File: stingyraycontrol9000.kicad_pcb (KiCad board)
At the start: 2 copper layers, 22.1 x 86.4 mm, 15 parts, among them J1 Screw_Terminal_01x04, J2 Screw_Terminal_01x04, J3 Screw_Terminal_01x02, J4 Conn_01x04, U1 ws2801, U2 LDD-L, U3 LDD-H

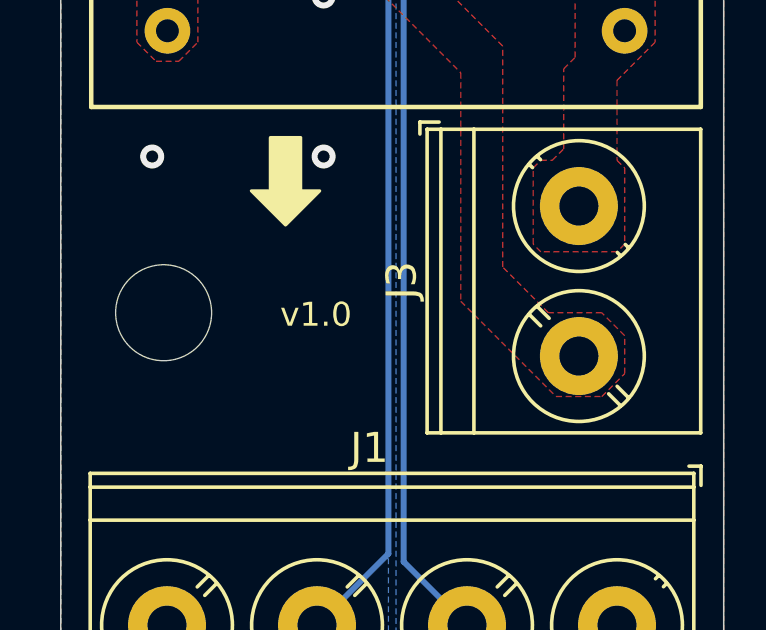
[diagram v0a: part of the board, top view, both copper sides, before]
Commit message: connect WS2801 polarity pin to ground and bump version to 1.1
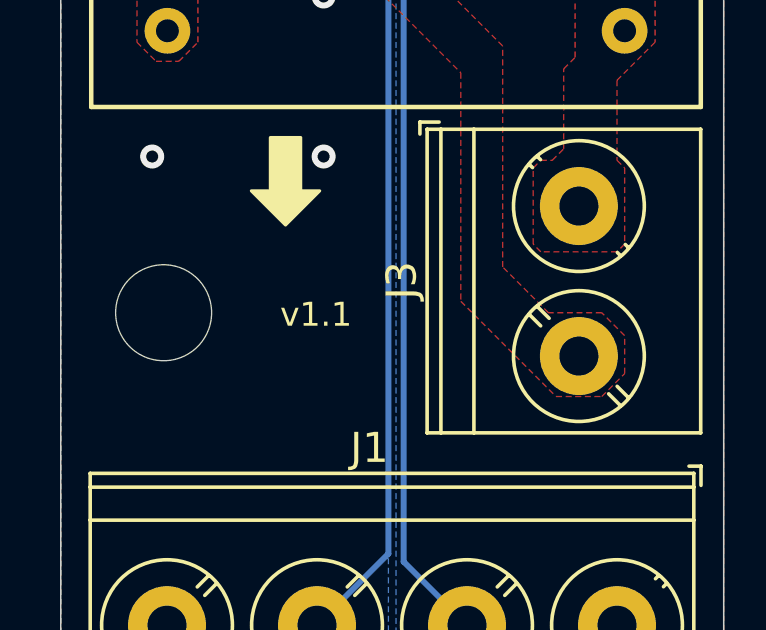
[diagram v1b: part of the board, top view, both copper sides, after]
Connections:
- U1 pad 3: (no net) -> GND
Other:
- board text added: "v1.1"
- board text removed: "v1.0"
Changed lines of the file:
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@@
     (pad 2 smd rect (at -2.7 -2.54) (size 1.5 0.6) (layers F.Cu F.Paste F.Mask)
       (net 2 /SDI))
-    (pad 3 smd rect (at -2.7 -1.27) (size 1.5 0.6) (layers F.Cu F.Paste F.Mask))
+    (pad 3 smd rect (at -2.7 -1.27) (size 1.5 0.6) (layers F.Cu F.Paste F.Mask)
+      (net 3 GND))
     (pad 4 smd rect (at -2.7 0) (size 1.5 0.6) (layers F.Cu F.Paste F.Mask)
       (net 3 GND))
@@
     )
   )
-  (gr_text v1.0 (at 135.001 135.9535) (layer F.SilkS)
+  (gr_text v1.1 (at 135.001 135.9535) (layer F.SilkS)
     (effects (font (size 0.8 0.8) (thickness 0.15)))
   )
@@
   (segment (start 135.048 86.995) (end 135.048 87.075) (width 0.2) (layer B.Cu) (net 1))
   (segment (start 135.255 86.788) (end 135.048 86.995) (width 0.2) (layer B.Cu) (net 1))
-  (segment (start 135.255 70.311) (end 135.255 86.788) (width 0.2) (layer B.Cu) (net 1))
-  (segment (start 135.048 70.104) (end 135.255 70.311) (width 0.2) (layer B.Cu) (net 1))
+  (segment (start 135.255 70.311) (end 135.255 86.788) (width 0.2) (layer B.Cu) (net 1) (status 10))
+  (segment (start 135.048 70.104) (end 135.255 70.311) (width 0.2) (layer B.Cu) (net 1) (status 30))
   (via (at 135.001 88.392) (size 0.6) (drill 0.3) (layers F.Cu B.Cu) (net 2))
   (segment (start 135.001 88.392) (end 133.698 88.392) (width 0.2) (layer F.Cu) (net 2) (status 20))
   (segment (start 135.655011 74.496989) (end 138.748001 71.403999) (width 0.2) (layer B.Cu) (net 2))
   (segment (start 135.001 88.392) (end 135.655011 87.737989) (width 0.2) (layer B.Cu) (net 2))
-  (segment (start 138.748001 71.403999) (end 140.048 70.104) (width 0.2) (layer B.Cu) (net 2))
+  (segment (start 138.748001 71.403999) (end 140.048 70.104) (width 0.2) (layer B.Cu) (net 2) (status 20))
   (segment (start 135.655011 87.737989) (end 135.655011 74.496989) (width 0.2) (layer B.Cu) (net 2))
   (via (at 135.255 125.349) (size 0.8) (drill 0.4) (layers F.Cu B.Cu) (net 3))
@@
   (segment (start 139.098 92.202) (end 142.748 92.202) (width 0.2) (layer F.Cu) (net 6) (status 10))
   (segment (start 147.447 90.297) (end 147.447 101.473) (width 0.2) (layer F.Cu) (net 6))
-  (segment (start 146.049999 102.870001) (end 145.288 103.632) (width 0.2) (layer F.Cu) (net 6))
+  (segment (start 146.049999 102.870001) (end 145.288 103.632) (width 0.2) (layer F.Cu) (net 6) (status 20))
   (segment (start 147.447 101.473) (end 146.049999 102.870001) (width 0.2) (layer F.Cu) (net 6))
-  (segment (start 146.05 88.9) (end 147.447 90.297) (width 0.2) (layer F.Cu) (net 6))
-  (segment (start 143.764 105.156) (end 145.288 103.632) (width 0.2) (layer F.Cu) (net 6))
+  (segment (start 146.05 88.9) (end 147.447 90.297) (width 0.2) (layer F.Cu) (net 6) (status 10))
+  (segment (start 143.764 105.156) (end 145.288 103.632) (width 0.2) (layer F.Cu) (net 6) (status 20))
   (segment (start 139.446 105.156) (end 143.764 105.156) (width 0.2) (layer F.Cu) (net 6))
   (segment (start 137.8966 103.6066) (end 139.446 105.156) (width 0.2) (layer F.Cu) (net 6))
-  (segment (start 136.3472 103.6066) (end 137.8966 103.6066) (width 0.2) (layer F.Cu) (net 6))
+  (segment (start 136.3472 103.6066) (end 137.8966 103.6066) (width 0.2) (layer F.Cu) (net 6) (status 10))
   (via (at 137.922 89.662) (size 0.6) (drill 0.3) (layers F.Cu B.Cu) (net 7))
-  (segment (start 137.922 89.662) (end 139.098 89.662) (width 0.2) (layer F.Cu) (net 7))
+  (segment (start 137.922 89.662) (end 139.098 89.662) (width 0.2) (layer F.Cu) (net 7) (status 20))
   (segment (start 138.303 102.489) (end 138.303 104.775) (width 0.2) (layer B.Cu) (net 7))
   (segment (start 137.922 102.108) (end 138.303 102.489) (width 0.2) (layer B.Cu) (net 7))
-  (segment (start 137.922 144.192) (end 140.034 146.304) (width 0.2) (layer B.Cu) (net 7))
+  (segment (start 137.922 144.192) (end 140.034 146.304) (width 0.2) (layer B.Cu) (net 7) (status 20))
   (segment (start 137.922 89.662) (end 137.922 102.108) (width 0.2) (layer B.Cu) (net 7))
   (segment (start 137.922 105.156) (end 137.922 144.192) (width 0.2) (layer B.Cu) (net 7))
   (segment (start 138.303 104.775) (end 137.922 105.156) (width 0.2) (layer B.Cu) (net 7))
   (via (at 137.922 88.392) (size 0.6) (drill 0.3) (layers F.Cu B.Cu) (net 8))
-  (segment (start 137.922 88.392) (end 139.098 88.392) (width 0.2) (layer F.Cu) (net 8))
+  (segment (start 137.922 88.392) (end 139.098 88.392) (width 0.2) (layer F.Cu) (net 8) (status 20))
   (segment (start 137.922 88.392) (end 137.287 89.027) (width 0.2) (layer B.Cu) (net 8))
   (segment (start 137.287 89.027) (end 137.287 90.043) (width 0.2) (layer B.Cu) (net 8))
   (segment (start 137.414 90.17) (end 137.414 102.235) (width 0.2) (layer B.Cu) (net 8))
   (segment (start 137.287 90.043) (end 137.414 90.17) (width 0.2) (layer B.Cu) (net 8))
-  (segment (start 137.414 143.924) (end 135.034 146.304) (width 0.2) (layer B.Cu) (net 8))
+  (segment (start 137.414 143.924) (end 135.034 146.304) (width 0.2) (layer B.Cu) (net 8) (status 20))
   (segment (start 137.414 104.9655) (end 137.414 143.924) (width 0.2) (layer B.Cu) (net 8))
   (segment (start 137.414 102.235) (end 137.8585 102.6795) (width 0.2) (layer B.Cu) (net 8))

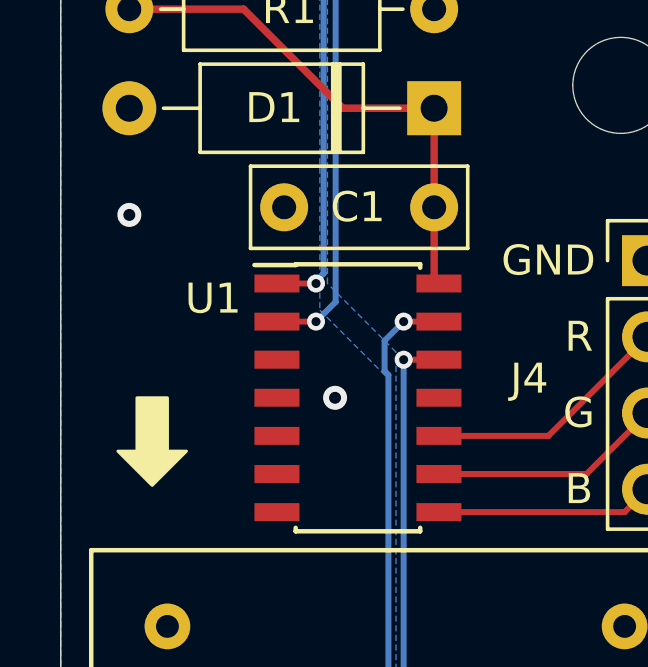
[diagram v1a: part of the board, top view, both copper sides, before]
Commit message: stingyraycontrol9000: add solder jumper for polarity selection
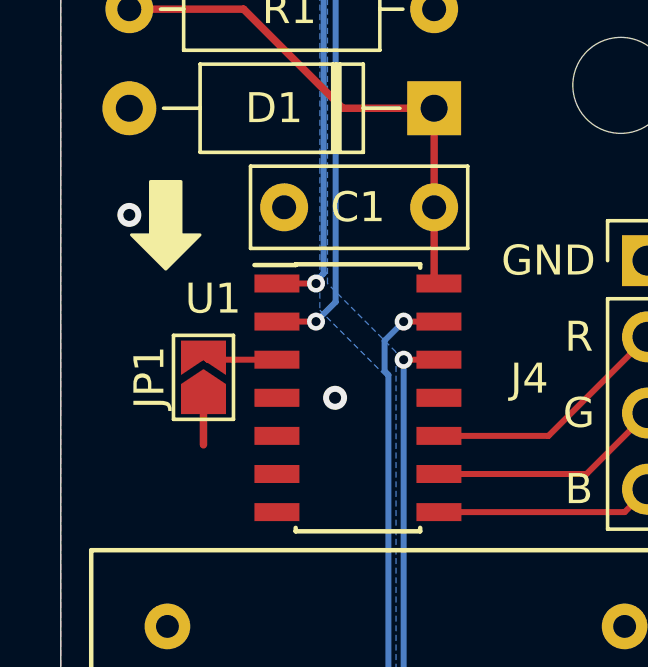
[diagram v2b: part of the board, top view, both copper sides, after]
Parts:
- added JP1: SolderJumper_2_Open, Jumper:SolderJumper-2_P1.3mm_Open_TrianglePad1.0x1.5mm, F.Cu at (131.2, 90.2)
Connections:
- U1 pad 3: GND -> /polarity
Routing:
- net /polarity: track 0.00 -> 2.50 mm
- net GND: track 0.00 -> 1.53 mm
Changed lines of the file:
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@@
-(kicad_pcb (version 20171130) (host pcbnew "(6.0.0-rc1-dev-1168-g71a2cd831)")
+(kicad_pcb (version 20171130) (host pcbnew "(5.1.0-rc2-47-g6eb84e42f)")
   (general
     (thickness 1.6)
     (drawings 26)
-    (tracks 60)
+    (tracks 63)
     (zones 0)
-    (modules 15)
-    (nets 13)
+    (modules 16)
+    (nets 14)
   )
   (page A4)
@@
     (solder_mask_min_width 0.25)
     (aux_axis_origin 0 0)
-    (visible_elements FFFFFF7F)
+    (visible_elements 7FFFFFFF)
     (pcbplotparams
       (layerselection 0x010f0_ffffffff)
@@
   (net 11 /LED-)
   (net 12 /LED+)
+  (net 13 /polarity)
   (net_class Default "This is the default net class."
     (clearance 0.2)
@@
     (uvia_dia 0.3)
     (uvia_drill 0.1)
+    (add_net /polarity)
   )
   (net_class data ""
@@
     (add_net /LED-)
     (add_net GND)
+  )
+  (module Jumper:SolderJumper-2_P1.3mm_Open_TrianglePad1.0x1.5mm (layer F.Cu)
+    (at 131.25 90.25 90)
+    (descr "SMD Solder Jumper, 1x1.5mm Triangular Pads, 0.3mm gap, open")
+    (tags "solder jumper open")
+    (attr virtual)
+    (fp_text reference JP1 (at 0 -1.8 90) (layer F.SilkS)
+      (effects (font (size 1 1) (thickness 0.15)))
+    )
+    (fp_text value SolderJumper_2_Open (at 0 1.9 90) (layer F.Fab)
+      (effects (font (size 1 1) (thickness 0.15)))
+    )
+    (fp_line (start -1.4 1) (end -1.4 -1) (layer F.SilkS) (width 0.12))
+    (fp_line (start 1.4 1) (end -1.4 1) (layer F.SilkS) (width 0.12))
+    (fp_line (start 1.4 -1) (end 1.4 1) (layer F.SilkS) (width 0.12))
+    (fp_line (start -1.4 -1) (end 1.4 -1) (layer F.SilkS) (width 0.12))
+    (fp_line (start -1.65 -1.25) (end 1.65 -1.25) (layer F.CrtYd) (width 0.05))
+    (fp_line (start -1.65 -1.25) (end -1.65 1.25) (layer F.CrtYd) (width 0.05))
+    (fp_line (start 1.65 1.25) (end 1.65 -1.25) (layer F.CrtYd) (width 0.05))
+    (fp_line (start 1.65 1.25) (end -1.65 1.25) (layer F.CrtYd) (width 0.05))
+    (pad 2 smd custom (at 0.725 0 90) (size 0.3 0.3) (layers F.Cu F.Mask)
+      (net 13 /polarity) (zone_connect 0)
+      (options (clearance outline) (anchor rect))
+      (primitives
+        (gr_poly (pts
+           (xy -0.65 -0.75) (xy 0.5 -0.75) (xy 0.5 0.75) (xy -0.65 0.75) (xy -0.15 0)
+) (width 0))
+      ))
+    (pad 1 smd custom (at -0.725 0 90) (size 0.3 0.3) (layers F.Cu F.Mask)
+      (net 3 GND) (zone_connect 0)
+      (options (clearance outline) (anchor rect))
+      (primitives
+        (gr_poly (pts
+           (xy -0.5 -0.75) (xy 0.5 -0.75) (xy 1 0) (xy 0.5 0.75) (xy -0.5 0.75)
+) (width 0))
+      ))
   )
   (module MountingHole:MountingHole_3.2mm_M3_ISO14580 (layer F.Cu)
@@
       (net 2 /SDI))
     (pad 3 smd rect (at -2.7 -1.27) (size 1.5 0.6) (layers F.Cu F.Paste F.Mask)
-      (net 3 GND))
+      (net 13 /polarity))
     (pad 4 smd rect (at -2.7 0) (size 1.5 0.6) (layers F.Cu F.Paste F.Mask)
       (net 3 GND))
@@
     (effects (font (size 1 1) (thickness 0.15)) (justify mirror))
   )
-  (gr_poly (pts (xy 129.032 90.932) (xy 130.048 90.932) (xy 130.048 92.71) (xy 130.683 92.71) (xy 129.54 93.853) (xy 128.397 92.71) (xy 129.032 92.71)) (layer F.SilkS) (width 0.1))
+  (gr_poly (pts (xy 129.484 83.722) (xy 130.5 83.722) (xy 130.5 85.5) (xy 131.135 85.5) (xy 129.992 86.643) (xy 128.849 85.5) (xy 129.484 85.5)) (layer F.SilkS) (width 0.1))
   (gr_poly (pts (xy 133.477 130.048) (xy 134.493 130.048) (xy 134.493 131.826) (xy 135.128 131.826) (xy 133.985 132.969) (xy 132.842 131.826) (xy 133.477 131.826)) (layer F.SilkS) (width 0.1))
   (gr_poly (pts (xy 137.033 135.509) (xy 138.049 135.509) (xy 138.049 137.287) (xy 138.684 137.287) (xy 137.541 138.43) (xy 136.398 137.287) (xy 137.033 137.287)) (layer B.SilkS) (width 0.1))
@@
   (via (at 135.636 90.932) (size 0.8) (drill 0.4) (layers F.Cu B.Cu) (net 3))
   (via (at 132.588 74.168) (size 0.8) (drill 0.4) (layers F.Cu B.Cu) (net 3))
+  (segment (start 131.25 90.975) (end 131.25 92.5) (width 0.25) (layer F.Cu) (net 3))
   (segment (start 145.288 94.742) (end 146.05 93.98) (width 0.2) (layer F.Cu) (net 4) (status 30))
   (segment (start 139.098 94.742) (end 145.288 94.742) (width 0.2) (layer F.Cu) (net 4) (status 30))
@@
   (segment (start 132.588 77.978) (end 135.89 81.28) (width 0.25) (layer F.Cu) (net 9))
   (segment (start 128.778 77.978) (end 132.588 77.978) (width 0.25) (layer F.Cu) (net 9) (status 10))
+  (segment (start 131.387 89.662) (end 131.25 89.525) (width 0.2) (layer F.Cu) (net 13))
+  (segment (start 133.698 89.662) (end 131.387 89.662) (width 0.2) (layer F.Cu) (net 13))
   (zone (net 3) (net_name GND) (layer F.Cu) (hatch edge 0.508)
     (connect_pads (clearance 0.2))
